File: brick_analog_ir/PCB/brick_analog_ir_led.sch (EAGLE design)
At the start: 5 parts

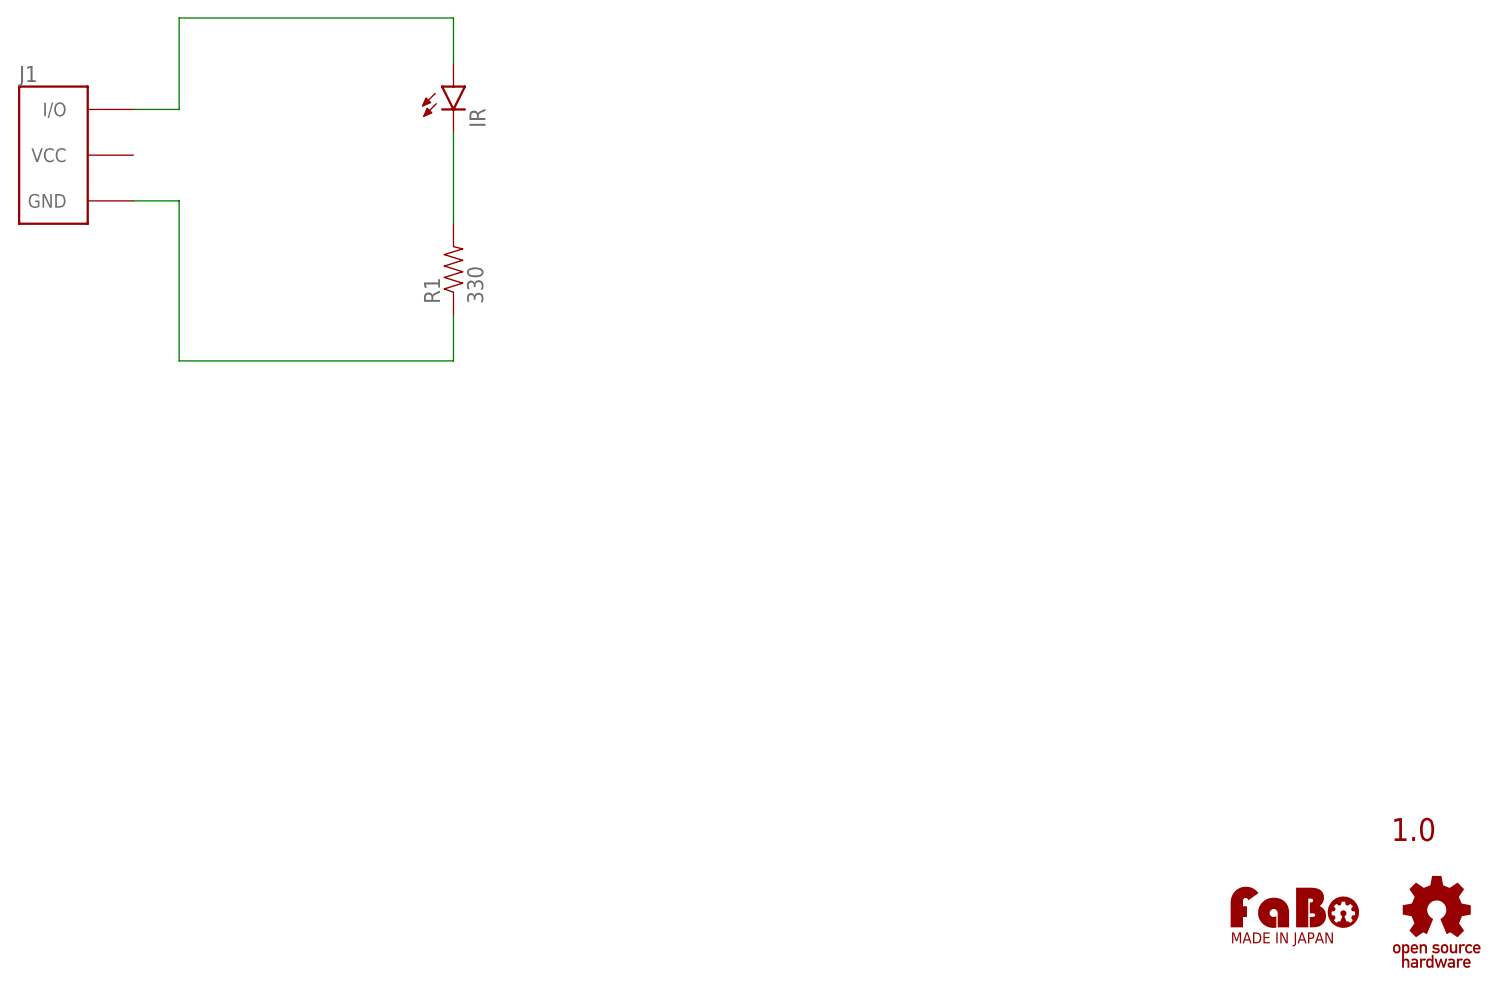
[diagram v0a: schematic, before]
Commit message: replace library brick_analog_ir
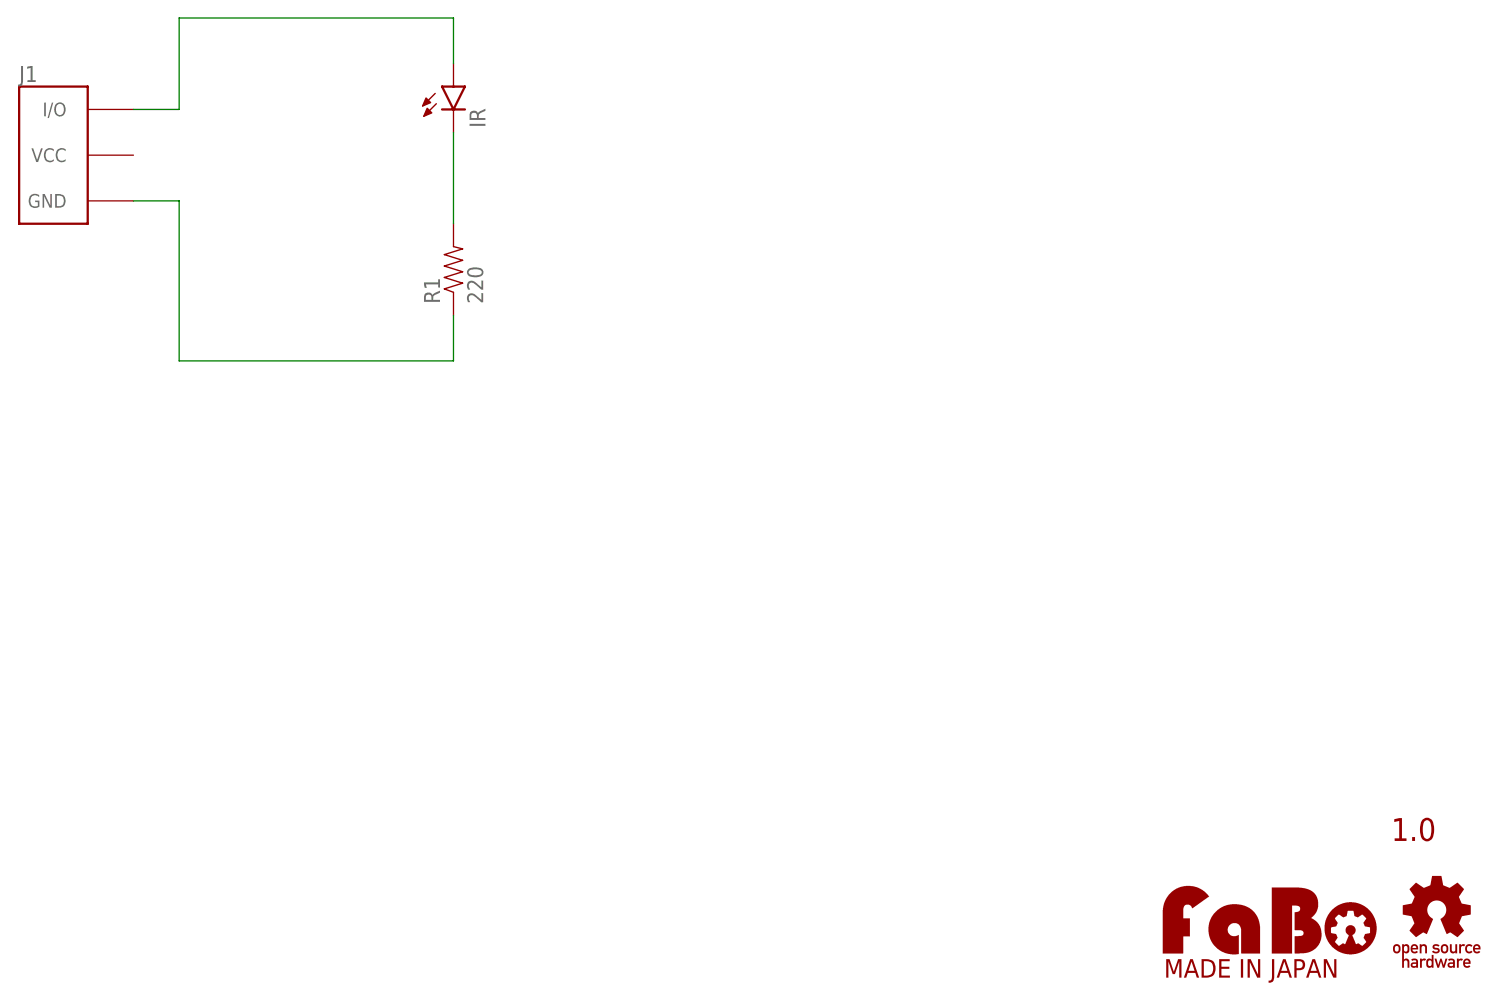
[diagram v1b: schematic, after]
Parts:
- IR: device GClue:LED-5MM -> FaBo-etc:LED-5MM
- J1: device GClue:BRICK_3PIN_NORMAL -> FaBo-Template:FABO_BRICK_3PIN
- R1: value 330 -> 220; device GClue:RES-PTH-REGULAR -> FaBo-etc:RES-PTH-REGULAR
- U$2: device FaBo:LOGO_FABO-M -> FaBo-etc:LOGO_FABO-M
- U$3: device GClue:LOGO_OSHW_T-M -> FaBo-etc:LOGO_OSHW-T_M
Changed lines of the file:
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@@
 </classes>
 <parts>
-<part name="U$1" library="GClue" deviceset="A4L-LOC" device=""/>
-<part name="U$2" library="FaBo" deviceset="LOGO_FABO" device="-M"/>
-<part name="U$3" library="GClue" deviceset="LOGO_OSHW_T" device="-M"/>
-<part name="J1" library="GClue" deviceset="BRICK_3PIN" device="_NORMAL"/>
-<part name="IR" library="GClue" deviceset="LED" device="-5MM"/>
-<part name="R1" library="GClue" deviceset="RES" device="-PTH-REGULAR" value="330"/>
+<part name="J1" library="FaBo-Template" deviceset="FABO_BRICK_3PIN" device=""/>
+<part name="IR" library="FaBo-etc" deviceset="LED" device="-5MM"/>
+<part name="R1" library="FaBo-etc" deviceset="RES" device="-PTH-REGULAR" value="220"/>
+<part name="U$1" library="FaBo-etc" deviceset="A4L-LOC" device=""/>
+<part name="U$2" library="FaBo-etc" deviceset="LOGO_FABO" device="-M"/>
+<part name="U$3" library="FaBo-etc" deviceset="LOGO_OSHW" device="-T_M"/>
 </parts>
 <sheets>
@@
 </plain>
 <instances>
-<instance part="U$1" gate="G$1" x="0" y="0"/>
-<instance part="U$2" gate="G$1" x="226.06" y="15.24"/>
-<instance part="U$3" gate="G$1" x="248.92" y="12.7"/>
 <instance part="J1" gate="G$1" x="96.52" y="96.52"/>
 <instance part="IR" gate="G$1" x="139.7" y="101.6"/>
 <instance part="R1" gate="G$1" x="139.7" y="83.82" rot="R90"/>
+<instance part="U$1" gate="G$1" x="0" y="0"/>
+<instance part="U$2" gate="G$1" x="218.44" y="5.08"/>
+<instance part="U$3" gate="G$1" x="248.92" y="12.7"/>
 </instances>
 <busses>
@@
 <net name="N$1" class="0">
 <segment>
-<pinref part="J1" gate="G$1" pin="I/O"/>
 <wire x1="104.14" y1="101.6" x2="109.22" y2="101.6" width="0.1524" layer="91"/>
 <wire x1="109.22" y1="101.6" x2="109.22" y2="111.76" width="0.1524" layer="91"/>
-<pinref part="IR" gate="G$1" pin="A"/>
 <wire x1="109.22" y1="111.76" x2="139.7" y2="111.76" width="0.1524" layer="91"/>
 <wire x1="139.7" y1="111.76" x2="139.7" y2="106.68" width="0.1524" layer="91"/>
+<pinref part="J1" gate="G$1" pin="I/O"/>
+<pinref part="IR" gate="G$1" pin="A"/>
 </segment>
 </net>
 <net name="N$2" class="0">
 <segment>
+<wire x1="139.7" y1="99.06" x2="139.7" y2="88.9" width="0.1524" layer="91"/>
 <pinref part="IR" gate="G$1" pin="C"/>
 <pinref part="R1" gate="G$1" pin="2"/>
-<wire x1="139.7" y1="99.06" x2="139.7" y2="88.9" width="0.1524" layer="91"/>
 </segment>
 </net>
 <net name="GND" class="0">
 <segment>
-<pinref part="J1" gate="G$1" pin="GND"/>
 <wire x1="104.14" y1="91.44" x2="109.22" y2="91.44" width="0.1524" layer="91"/>
 <wire x1="109.22" y1="91.44" x2="109.22" y2="73.66" width="0.1524" layer="91"/>
 <wire x1="109.22" y1="73.66" x2="139.7" y2="73.66" width="0.1524" layer="91"/>
+<wire x1="139.7" y1="73.66" x2="139.7" y2="78.74" width="0.1524" layer="91"/>
+<pinref part="J1" gate="G$1" pin="GND"/>
 <pinref part="R1" gate="G$1" pin="1"/>
-<wire x1="139.7" y1="73.66" x2="139.7" y2="78.74" width="0.1524" layer="91"/>
 </segment>
 </net>

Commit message: change Revision
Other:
- note added: "1.0.0"
- note removed: "1.0"
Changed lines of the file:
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@@
 <?xml version="1.0" encoding="utf-8"?>
 <!DOCTYPE eagle SYSTEM "eagle.dtd">
-<eagle version="7.3.0">
+<eagle version="7.4.0">
 <drawing>
 <settings>
@@
 <sheet>
 <plain>
-<text x="246.38" y="20.32" size="2.54" layer="94" align="bottom-center">1.0</text>
+<text x="246.38" y="20.32" size="2.54" layer="94" align="bottom-center">1.0.0</text>
 </plain>
 <instances>
